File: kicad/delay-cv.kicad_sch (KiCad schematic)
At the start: 27 parts, among them Q15 2N3904, Q16 2N3904, U20 TL074

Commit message: component positioning mostly done
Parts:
- C60, C61, C62, C63, C64, C65: footprint rumblesan-standard-parts:C_Rect_L7.0mm_W3.5mm_P5.00mm -> rumblesan-standard-parts:C_Rect_L7.0mm_W2.5mm_P5.00mm
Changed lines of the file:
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@@
     (property "Reference" "C62" (id 0) (at 182.88 88.8492 90))
     (property "Value" "10pF" (id 1) (at 182.88 91.1606 90))
-    (property "Footprint" "rumblesan-standard-parts:C_Rect_L7.0mm_W3.5mm_P5.00mm" (id 2) (at 184.15 100.965 0)
+    (property "Footprint" "rumblesan-standard-parts:C_Rect_L7.0mm_W2.5mm_P5.00mm" (id 2) (at 184.15 100.965 0)
       (effects (font (size 1.27 1.27)) hide)
     )
@@
     (property "Reference" "C60" (id 0) (at 76.2 72.3392 90))
     (property "Value" "10pF" (id 1) (at 76.2 74.6506 90))
-    (property "Footprint" "rumblesan-standard-parts:C_Rect_L7.0mm_W3.5mm_P5.00mm" (id 2) (at 77.47 84.455 0)
+    (property "Footprint" "rumblesan-standard-parts:C_Rect_L7.0mm_W2.5mm_P5.00mm" (id 2) (at 77.47 84.455 0)
       (effects (font (size 1.27 1.27)) hide)
     )
@@
       (effects (font (size 1.27 1.27)) (justify left))
     )
-    (property "Footprint" "rumblesan-standard-parts:C_Rect_L7.0mm_W3.5mm_P5.00mm" (id 2) (at 142.875 152.4 90)
+    (property "Footprint" "rumblesan-standard-parts:C_Rect_L7.0mm_W2.5mm_P5.00mm" (id 2) (at 142.875 152.4 90)
       (effects (font (size 1.27 1.27)) hide)
     )
@@
     (property "Reference" "C61" (id 0) (at 142.24 73.6092 90))
     (property "Value" "10pF" (id 1) (at 142.24 75.9206 90))
-    (property "Footprint" "rumblesan-standard-parts:C_Rect_L7.0mm_W3.5mm_P5.00mm" (id 2) (at 143.51 85.725 0)
+    (property "Footprint" "rumblesan-standard-parts:C_Rect_L7.0mm_W2.5mm_P5.00mm" (id 2) (at 143.51 85.725 0)
       (effects (font (size 1.27 1.27)) hide)
     )
@@
     (property "Reference" "C63" (id 0) (at 218.44 109.1692 90))
     (property "Value" "100pF" (id 1) (at 218.44 111.4806 90))
-    (property "Footprint" "rumblesan-standard-parts:C_Rect_L7.0mm_W3.5mm_P5.00mm" (id 2) (at 217.17 109.855 0)
+    (property "Footprint" "rumblesan-standard-parts:C_Rect_L7.0mm_W2.5mm_P5.00mm" (id 2) (at 217.17 109.855 0)
       (effects (font (size 1.27 1.27)) hide)
     )
@@
       (effects (font (size 1.27 1.27)) (justify left))
     )
-    (property "Footprint" "rumblesan-standard-parts:C_Rect_L7.0mm_W3.5mm_P5.00mm" (id 2) (at 142.875 165.1 90)
-      (effects (font (size 1.27 1.27)) hide)
-    )
+    (property "Footprint" "rumblesan-standard-parts:C_Rect_L7.0mm_W2.5mm_P5.00mm" (id 2) (at 142.875 165.1 90)
+      (effects (font (size 1.27 1.27)) hide)
+    )

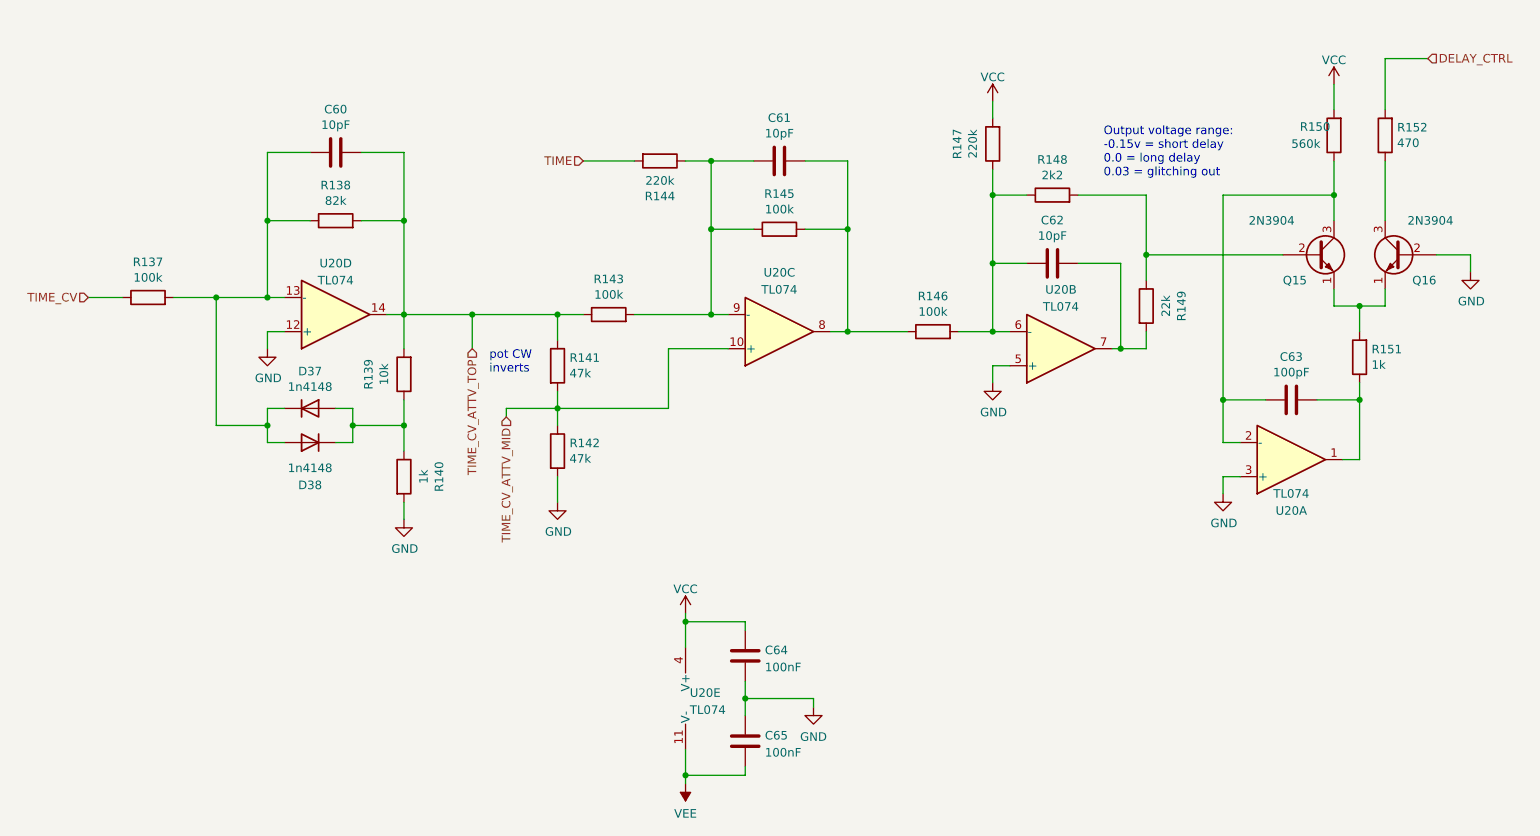
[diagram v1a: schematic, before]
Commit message: Full rejig to use attiny for divider
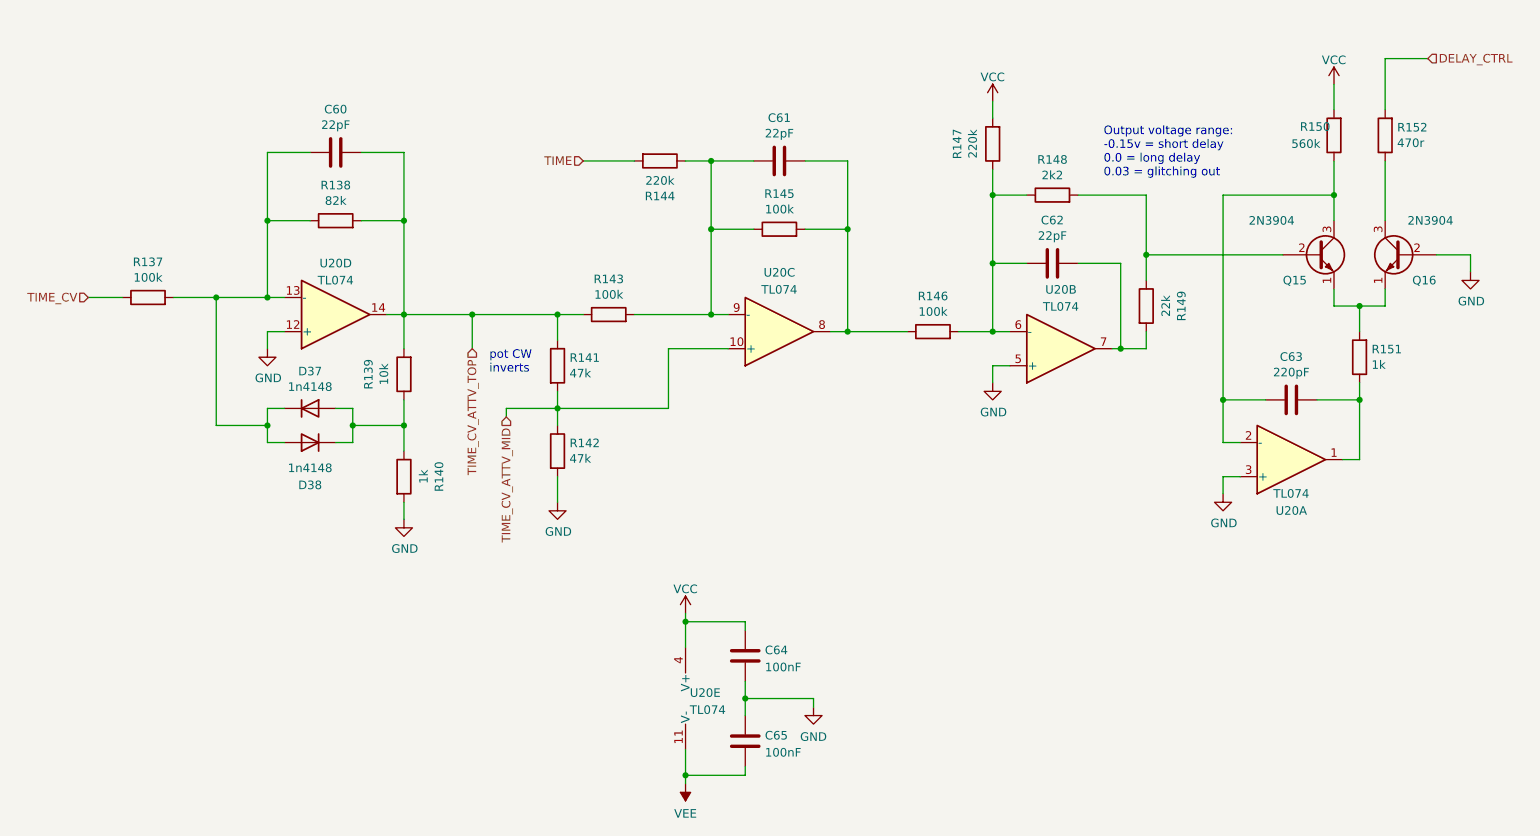
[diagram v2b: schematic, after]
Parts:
- C60, C61, C62: value 10pF -> 22pF
- C63: value 100pF -> 220pF
- C64, C65: Spec ceramic C0G -> ceramic X7R
- R152: value 470 -> 470r
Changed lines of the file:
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@@
     (in_bom yes) (on_board yes)
     (property "Reference" "C62" (id 0) (at 182.88 88.8492 90))
-    (property "Value" "10pF" (id 1) (at 182.88 91.1606 90))
+    (property "Value" "22pF" (id 1) (at 182.88 91.1606 90))
     (property "Footprint" "rumblesan-standard-parts:C_Rect_L7.0mm_W2.5mm_P5.00mm" (id 2) (at 184.15 100.965 0)
       (effects (font (size 1.27 1.27)) hide)
@@
     (in_bom yes) (on_board yes)
     (property "Reference" "C60" (id 0) (at 76.2 72.3392 90))
-    (property "Value" "10pF" (id 1) (at 76.2 74.6506 90))
+    (property "Value" "22pF" (id 1) (at 76.2 74.6506 90))
     (property "Footprint" "rumblesan-standard-parts:C_Rect_L7.0mm_W2.5mm_P5.00mm" (id 2) (at 77.47 84.455 0)
       (effects (font (size 1.27 1.27)) hide)
@@
       (effects (font (size 1.27 1.27)) hide)
     )
-    (property "Spec" "ceramic C0G" (id 4) (at 140.97 153.67 90)
+    (property "Spec" "ceramic X7R" (id 4) (at 140.97 153.67 90)
       (effects (font (size 1.27 1.27)) hide)
     )
@@
     (in_bom yes) (on_board yes)
     (property "Reference" "C61" (id 0) (at 142.24 73.6092 90))
-    (property "Value" "10pF" (id 1) (at 142.24 75.9206 90))
+    (property "Value" "22pF" (id 1) (at 142.24 75.9206 90))
     (property "Footprint" "rumblesan-standard-parts:C_Rect_L7.0mm_W2.5mm_P5.00mm" (id 2) (at 143.51 85.725 0)
       (effects (font (size 1.27 1.27)) hide)
@@
     (in_bom yes) (on_board yes)
     (property "Reference" "C63" (id 0) (at 218.44 109.1692 90))
-    (property "Value" "100pF" (id 1) (at 218.44 111.4806 90))
+    (property "Value" "220pF" (id 1) (at 218.44 111.4806 90))
     (property "Footprint" "rumblesan-standard-parts:C_Rect_L7.0mm_W2.5mm_P5.00mm" (id 2) (at 217.17 109.855 0)
       (effects (font (size 1.27 1.27)) hide)
@@
       (effects (font (size 1.27 1.27)) (justify left))
     )
-    (property "Value" "470" (id 1) (at 234.188 77.343 0)
+    (property "Value" "470r" (id 1) (at 234.188 77.343 0)
       (effects (font (size 1.27 1.27)) (justify left))
     )
@@
       (effects (font (size 1.27 1.27)) hide)
     )
-    (property "Spec" "ceramic C0G" (id 4) (at 140.97 166.37 90)
-      (effects (font (size 1.27 1.27)) hide)
-    )
+    (property "Spec" "ceramic X7R" (id 4) (at 140.97 166.37 90)
+      (effects (font (size 1.27 1.27)) hide)
+    )

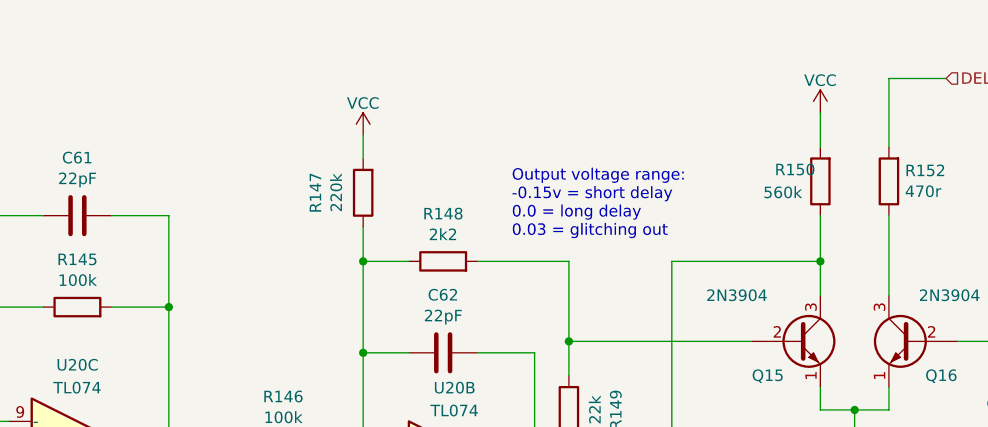
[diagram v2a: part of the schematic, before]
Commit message: Layout seems to be all done, though needs further checking
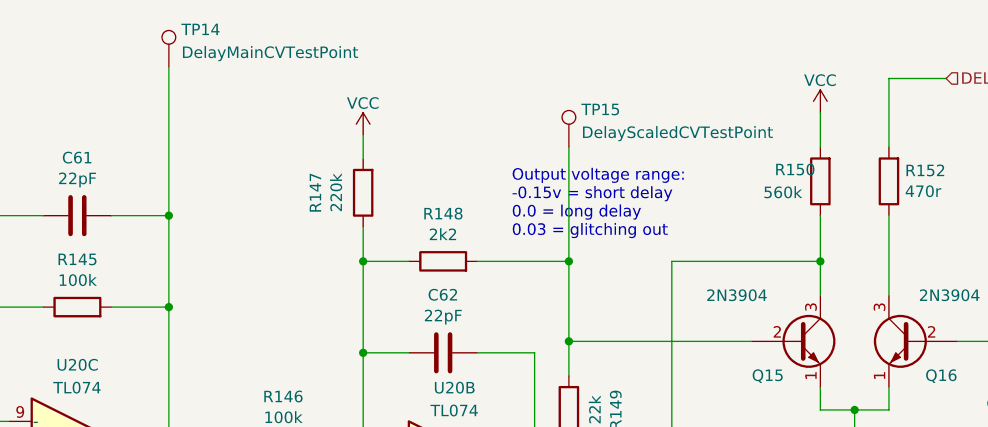
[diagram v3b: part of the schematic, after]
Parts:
- added TP14: DelayMainCVTestPoint, rumblesan-standard-parts:TestPoint_Loop_D2.50mm_Drill1.0mm_LowProfile, symbol Connector:TestPoint
- added TP15: DelayScaledCVTestPoint, rumblesan-standard-parts:TestPoint_Loop_D2.50mm_Drill1.0mm_LowProfile, symbol Connector:TestPoint
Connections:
- net at Q15.2 (B), R148.2, R149.1: now also TP15.1
- net at C61.1, R145.2, R146.1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: now also TP14.1
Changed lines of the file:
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@@
   (junction (at 132.08 80.01) (diameter 0) (color 0 0 0 0)
   )
+  (junction (at 196.85 85.09) (diameter 0) (color 0 0 0 0)
+  )
   (junction (at 78.74 119.38) (diameter 0) (color 0 0 0 0)
   )
@@
   (junction (at 66.04 100.33) (diameter 0) (color 0 0 0 0)
   )
+  (junction (at 152.4 80.01) (diameter 0) (color 0 0 0 0)
+  )
   (junction (at 193.04 107.95) (diameter 0) (color 0 0 0 0)
   )
@@
     (stroke (width 0) (type default) (color 0 0 0 0))
   )
+  (wire (pts (xy 196.85 72.39) (xy 196.85 85.09))
+    (stroke (width 0) (type default) (color 0 0 0 0))
+  )
   (wire (pts (xy 191.77 107.95) (xy 193.04 107.95))
     (stroke (width 0) (type default) (color 0 0 0 0))
@@
   )
   (wire (pts (xy 217.17 93.98) (xy 196.85 93.98))
+    (stroke (width 0) (type default) (color 0 0 0 0))
+  )
+  (wire (pts (xy 152.4 63.5) (xy 152.4 80.01))
     (stroke (width 0) (type default) (color 0 0 0 0))
   )
@@
     (pin "1")
     (pin "2")
+  )
+  (symbol (lib_id "Connector:TestPoint") (at 196.85 72.39 0) (unit 1)
+    (in_bom yes) (on_board yes) (fields_autoplaced)
+    (property "Reference" "TP15" (id 0) (at 198.247 68.2533 0)
+      (effects (font (size 1.27 1.27)) (justify left))
+    )
+    (property "Value" "DelayScaledCVTestPoint" (id 1) (at 198.247 70.7902 0)
+      (effects (font (size 1.27 1.27)) (justify left))
+    )
+    (property "Footprint" "rumblesan-standard-parts:TestPoint_Loop_D2.50mm_Drill1.0mm_LowProfile" (id 2) (at 201.93 72.39 0)
+      (effects (font (size 1.27 1.27)) hide)
+    )
+    (property "Datasheet" "~" (id 3) (at 201.93 72.39 0)
+      (effects (font (size 1.27 1.27)) hide)
+    )
+    (pin "1")
   )
   (symbol (lib_id "Device:D") (at 72.39 116.84 0) (unit 1)
@@
     (pin "2")
   )
+  (symbol (lib_id "Connector:TestPoint") (at 152.4 63.5 0) (unit 1)
+    (in_bom yes) (on_board yes) (fields_autoplaced)
+    (property "Reference" "TP14" (id 0) (at 153.797 59.3633 0)
+      (effects (font (size 1.27 1.27)) (justify left))
+    )
+    (property "Value" "DelayMainCVTestPoint" (id 1) (at 153.797 61.9002 0)
+      (effects (font (size 1.27 1.27)) (justify left))
+    )
+    (property "Footprint" "rumblesan-standard-parts:TestPoint_Loop_D2.50mm_Drill1.0mm_LowProfile" (id 2) (at 157.48 63.5 0)
+      (effects (font (size 1.27 1.27)) hide)
+    )
+    (property "Datasheet" "~" (id 3) (at 157.48 63.5 0)
+      (effects (font (size 1.27 1.27)) hide)
+    )
+    (pin "1")
+  )
   (symbol (lib_id "power:GND") (at 86.36 133.35 0) (unit 1)

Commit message: Changing name to the mercurial machine
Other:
- title: (none) -> The Mercurial Machine
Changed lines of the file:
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@@
   (paper "A4")
   (title_block
+    (title "The Mercurial Machine")
+    (date "2023-05-13")
+    (rev "r02")
     (comment 2 "creativecommons.org/licenses/by/4.0/")
     (comment 3 "License: CC BY 4.0")

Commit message: geographically reannotate parts
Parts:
- renumbered C60 to C31, C63 to C33, C65 to C35, C64 to C37, C62 to C39, C61 to C40, D37 to D10, D38 to D12, Q16 to Q4, Q15 to Q5, R152 to R55, R137 to R57, R141 to R58, R142 to R61, R143 to R65, R150 to R66, R151 to R75, R138 to R76, R144 to R77, R145 to R78, R149 to R79, R140 to R81, R139 to R82, R146 to R83, R148 to R84, R147 to R85, TP15 to TP12, TP14 to TP8, U20 to U7

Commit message: Changing name again
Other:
- title: The Mercurial Machine -> Ouroboros
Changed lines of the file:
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@@
   (paper "A4")
   (title_block
-    (title "The Mercurial Machine")
+    (title "Ouroboros")
     (date "2023-05-13")
     (rev "r02")

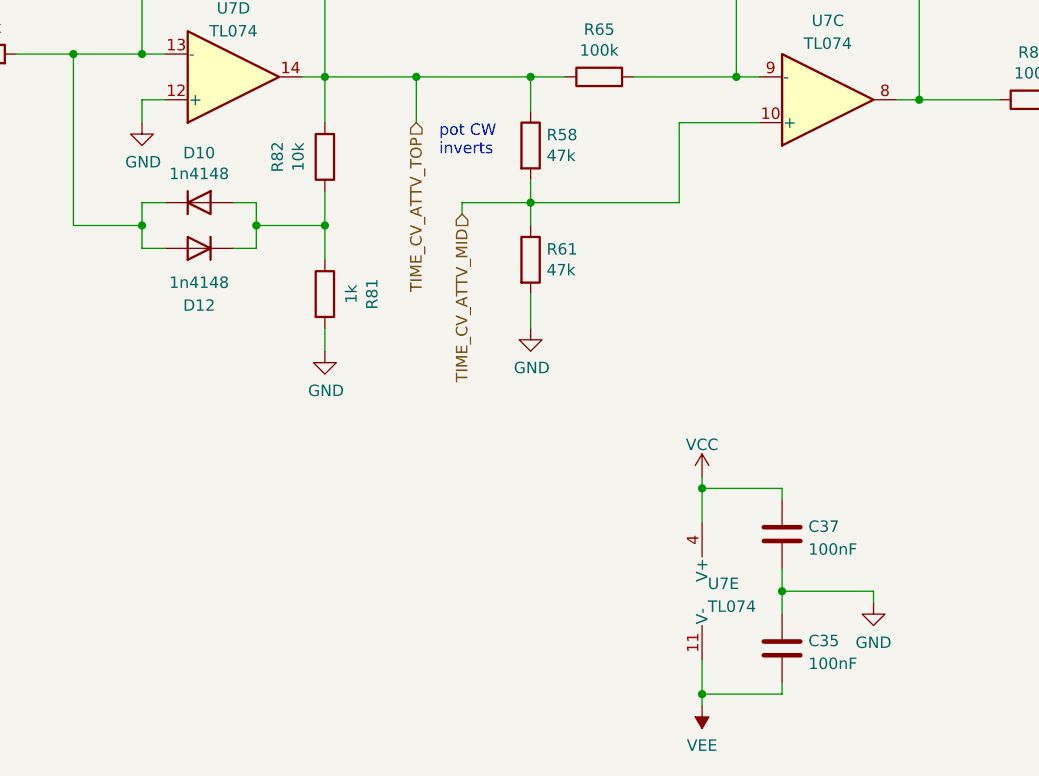
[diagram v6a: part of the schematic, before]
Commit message: Updating for kicad 7
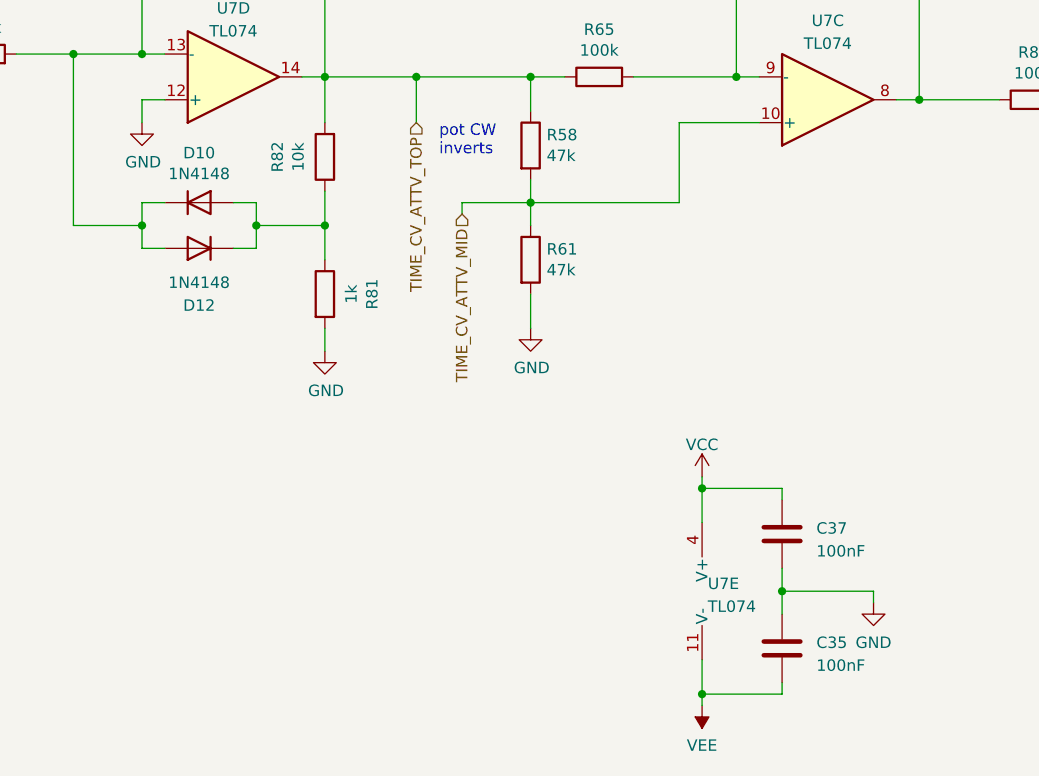
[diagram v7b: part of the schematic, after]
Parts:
- C31, C33, C39, C40: footprint rumblesan-standard-parts:C_Rect_L7.0mm_W2.5mm_P5.00mm -> Rumblesan_Standard_Parts:C_Rect_L7.0mm_W2.5mm_P5.00mm; symbol rumblesan-standard-parts:C -> Rumblesan Standard Parts:C
- C35, C37: footprint rumblesan-standard-parts:C_Rect_L7.0mm_W2.5mm_P5.00mm -> Rumblesan_Standard_Parts:C_Rect_L7.0mm_W2.5mm_P5.00mm; symbol rumblesan-standard-parts:C -> Rumblesan Standard Parts:C; Spec ceramic X7R -> ceramic C0G
- D10, D12: value 1n4148 -> 1N4148; footprint rumblesan-standard-parts:D_DO-35_SOD27_P7.62mm_Horizontal -> Rumblesan_Standard_Parts:D_DO-35_SOD27_P7.62mm_Horizontal
- Q4, Q5: footprint rumblesan-standard-parts:TO-92_Inline_Wide -> Rumblesan_Standard_Parts:TO-92_Inline_Wide
- R55, R57, R58, R61, R65, R66, R75, R76, R77, R78, R79, R81, R82, R83, R84, R85: footprint rumblesan-standard-parts:R_Axial_DIN0207_L6.3mm_D2.5mm_P10.16mm_Horizontal -> Rumblesan_Standard_Parts:R_Axial_DIN0207_L6.3mm_D2.5mm_P10.16mm_Horizontal; symbol rumblesan-standard-parts:R -> Rumblesan Standard Parts:R
- TP12, TP8: footprint rumblesan-standard-parts:TestPoint_Loop_D2.50mm_Drill1.0mm_LowProfile -> Rumblesan_Standard_Parts:TestPoint_Loop_D2.50mm_Drill1.0mm_LowProfile
- U7: footprint rumblesan-standard-parts:DIP-14_W7.62mm_Socket -> Rumblesan_Standard_Parts:DIP-14_W7.62mm_Socket

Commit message: Minor tweaks to rev2 values
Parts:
- R57: value 100k -> 120k
- R76: value 82k -> 100k
- R79: value 22k -> 20k
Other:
- note added: "Vout = -2k7((Vcc/220k) + (cv/100k))"
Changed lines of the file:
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@@
     (stroke (width 0) (type default))
+  )
+  (text "Vout = -2k7((Vcc/220k) + (cv/100k))" (at 158.75 124.46 0)
+    (effects (font (size 1.27 1.27)) (justify left bottom))
   )
   (text "Output voltage range:\n-0.15v = short delay\n0.0 = long delay\n0.03 = glitching out"
@@
       (effects (font (size 1.27 1.27)))
     )
-    (property "Value" "82k" (at 76.2 85.9536 90)
+    (property "Value" "100k" (at 76.2 85.9536 90)
       (effects (font (size 1.27 1.27)))
     )
@@
       (effects (font (size 1.27 1.27)))
     )
-    (property "Value" "22k" (at 199.7964 101.6 90)
+    (property "Value" "20k" (at 199.7964 101.6 90)
       (effects (font (size 1.27 1.27)))
     )
@@
       (effects (font (size 1.27 1.27)))
     )
-    (property "Value" "100k" (at 48.26 97.3836 90)
-      (effects (font (size 1.27 1.27)))
-    )
+    (property "Value" "120k" (at 48.26 97.3836 90)
+      (effects (font (size 1.27 1.27)))
+    )
